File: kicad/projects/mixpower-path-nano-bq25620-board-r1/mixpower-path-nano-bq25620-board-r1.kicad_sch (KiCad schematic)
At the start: 73 parts, among them J1 USB_C_Receptacle_HRO_TYPE-C-3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, J2 USB_C_Receptacle_HRO_TYPE-C-3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, J3 JST-PH2, J4 LED_STRIP, Q1 SIA931DJ, Q2 AO3401A, Q3 FS8205A, U1 STUSB4500QTR, U2 MCP73831-4-MC, U3 TPS61088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

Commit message: feat: rework schematics and add proper calculations
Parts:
- removed C10, C15: 22u, symbol Device:C_Small
- removed C11, C13: 100n, symbol Device:C_Small
- removed C12, C14: 10u, symbol Device:C_Small
- removed C16, C19, C21, C9: 1u, symbol Device:C_Small
- removed C17: 100n, Capacitor_SMD:C_0402_1005Metric, symbol Device:C_Small
- removed C18: 4.7n, symbol Device:C_Small
- removed C20: 47n, symbol Device:C_Small
- removed C22, C23: 47u, symbol Device:C_Small
- removed D4: SS36, Diode_SMD:D_SMA, symbol mixlib-discrete-schottkydiode:SS36
- removed D5: ESD5Z5.0T1G, Diode_SMD:D_SOD-523, symbol Diode:ESD5Zxx
- removed D6, D7: LED, symbol Device:LED_Small
- removed J2: USB_C_Receptacle_HRO_TYPE-C-31-M-12, Connector_USB:USB_C_Receptacle_HRO_TYPE-C-31-M-12, symbol Connector:USB_C_Receptacle_USB2.0_16P
- removed J3: JST-PH2, symbol Connector_Generic:Conn_01x02
- removed J4: LED_STRIP, symbol Connector_Generic:Conn_01x02
- removed L1: 10u, symbol Device:L_Small
- removed Q2: AO3401A, Package_TO_SOT_SMD:SOT-23, symbol mixlib-discrete-mosfet:AO3401A
- removed Q3: FS8205A, mixlib-discrete-mosfet:Specific_FS8205A, symbol mixlib-discrete-mosfet:FS8205A
- removed R11: 100k, Resistor_SMD:R_0402_1005Metric, symbol Device:R_Small
- removed R12, R13: 5.1k, Resistor_SMD:R_0402_1005Metric, symbol Device:R_Small
- removed R14, R22, R23: 3k, symbol Device:R_Small
- removed R15, R20: 150k, symbol Device:R_Small
- removed R16: 100, Resistor_SMD:R_0402_1005Metric, symbol Device:R_Small
- removed R17: 220k, symbol Device:R_Small
- removed R18: 13k, symbol Device:R_Small
- removed R19: 1k, Resistor_SMD:R_0402_1005Metric, symbol Device:R_Small
- removed R21: 56k, symbol Device:R_Small
- removed RV1: 360k, symbol Device:R_Potentiometer_Small
- removed U2: MCP73831-4-MC, Package_DFN_QFN:DFN-8-1EP_3x2mm_P0.5mm_EP1.7x1.4mm, symbol Battery_Management:MCP73831-4-MC
- removed U3: TPS61088, Package_DFN_QFN:Texas_VQFN-RNR0011A-11, symbol Regulator_Switching:TPS61089
- removed U4: DW01A, Package_TO_SOT_SMD:SOT-23-6, symbol Battery_Management:DW01A
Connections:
- no-connect marks 17 -> 8
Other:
- note added: "* On battery, 5V can only be provided by OTG mode. * ADC enablement is necessary for measurement of voltages (VBUS, VBAT) and currents (IBUS and IBAT)."
- note removed: "* Configured for output voltage: 9V - 12V * When Rpot is 0, R1 = 360K, then Vout = 9V * When Rpot is 150k, R1 = 510K, then Vout >= 12V"
- note removed: "* If you can't find 25V-rated capacitors, substitute for a smaller value with appropriate rating, e.g. 3x22uF @ 25V. The higher, the better. Tantalum capacitors are perhaps better."
- note removed: "* PGND and AGND both directly to GND."
- note removed: "* Pins: 1, 8"
- note removed: "* Pins: 2, 3"
- note removed: "* Pins: 6, 7"
- note removed: "* Place all capacitors here near the charger."
- note removed: "* Place near the IC."
- note removed: "* Place near the IC. Keep loops small in the PCB."
- note removed: "* Place near the USB connector."
- note removed: "* Please check all the calculations from the datasheet. I only copied the values you provided, with a few changes here and there."
- note removed: "* This is a two-input power input selector. * If USB-C is disconnected, VBUS will be missing. The base of the MOSFET will be 0V due to the base resistor R11. In this configuration, the MOSFET will allow VBAT to pass through, with very little resistance. * However, if USB-C is connected, VBUS will be present, and at 5V. This will make Vgs >= 0. Vgs must be negative in order for the MOSFET to close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"
- note removed: "12V BOOST CONVERTER"
- note removed: "BATTERY CHARGER"
- note removed: "BATTERY PROTECTION & CONNECTOR"
- note removed: "BOOST CONVERTER INPUT POWER SELECTOR"
- note removed: "INDICATOR LEDS & LED STRIP CONNECTOR"
- note removed: "TODO: REVISE TABLE VALUES"
- note removed: "USB-C CONNECTOR"

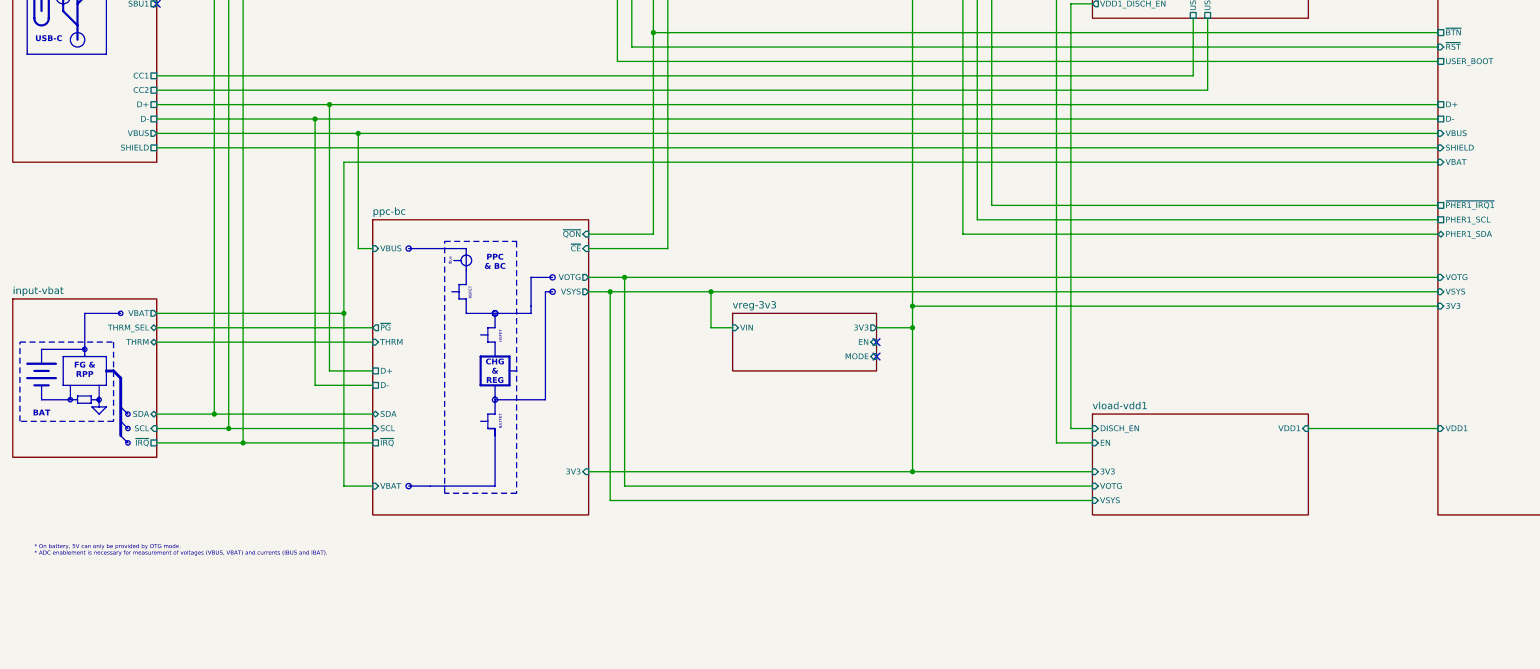
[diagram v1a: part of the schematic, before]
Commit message: fix: put all subsheets in root of the Kicad project, regenerate schematics plots
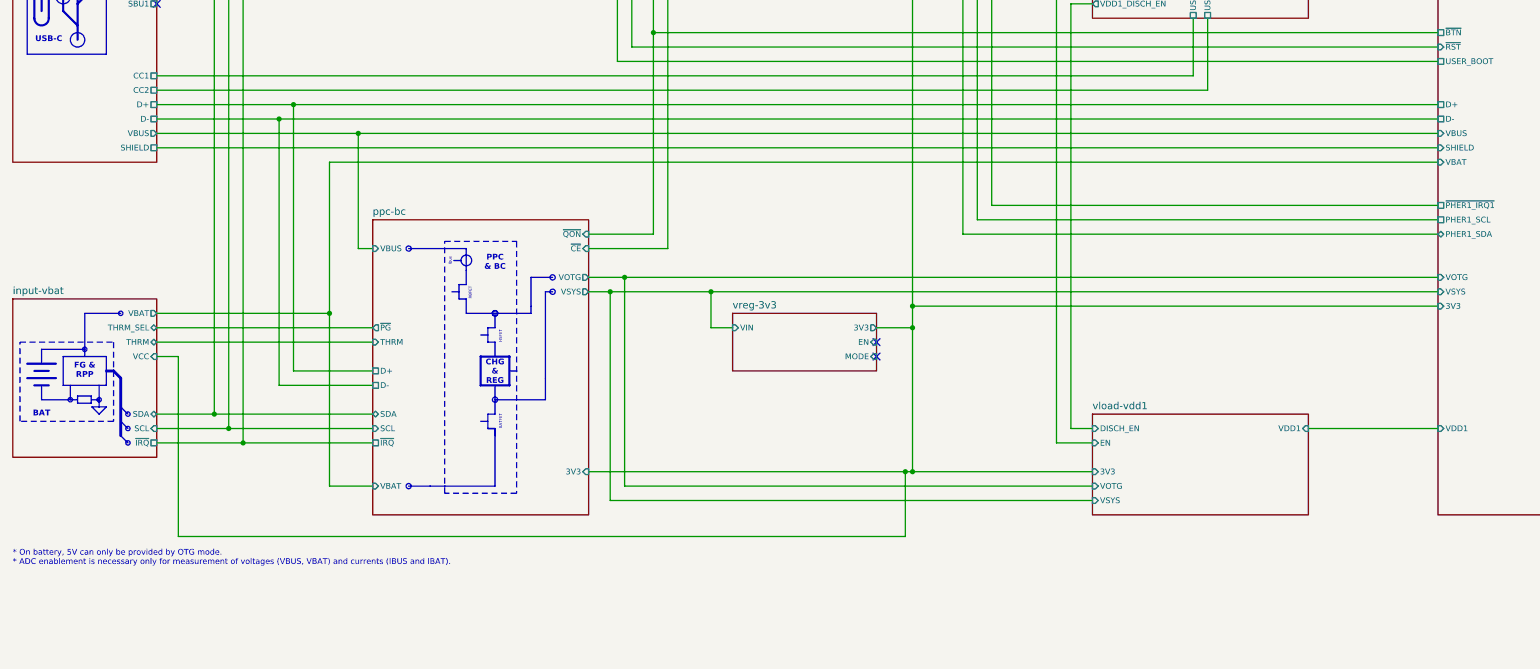
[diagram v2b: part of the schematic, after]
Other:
- sheet input-vbat: file sheets/input-vbat.kicad_sch -> subsheet__input-vbat.kicad_sch
- sheet input-vbat ports: added VCC; removed none
- sheet input-vbus: file sheets/input-vbus.kicad_sch -> subsheet__input-vbus.kicad_sch
- sheet output-headers: file sheets/output-headers.kicad_sch -> subsheet__output-headers.kicad_sch
- sheet ppc-bc: file sheets/ppc-bc.kicad_sch -> subsheet__ppc-bc.kicad_sch
- sheet soc-control: file sheets/soc-control.kicad_sch -> subsheet__soc-control.kicad_sch
- sheet util-buttons: file sheets/util-buttons.kicad_sch -> subsheet__util-buttons.kicad_sch
- sheet vload-vdd1: file sheets/vload-vdd1.kicad_sch -> subsheet__vload-vdd1.kicad_sch
- sheet vreg-3v3: file sheets/vreg-3v3.kicad_sch -> subsheet__vreg-3v3.kicad_sch
- note added: "* On battery, 5V can only be provided by OTG mode. * ADC enablement is necessary only for measurement of voltages (VBUS, VBAT) and currents (IBUS and IBAT)."
- note removed: "* On battery, 5V can only be provided by OTG mode. * ADC enablement is necessary for measurement of voltages (VBUS, VBAT) and currents (IBUS and IBAT)."
- title: (none) -> mixpower-path-nano-bq25620-board
